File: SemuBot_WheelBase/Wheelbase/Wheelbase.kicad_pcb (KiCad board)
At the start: 2 copper layers, 100 x 80 mm, 120 parts, among them IC1 DRV8353FSRTAR, IC2 DRV8353FSRTAR, IC3 DRV8353FSRTAR, J1 10155435-00011LF, J10 B5B-XH-A_LF__SN_, J11 B5B-XH-A_LF__SN_, J12 B5B-XH-A_LF__SN_, J13 MTSW-104-09-L-S-400, J14 XT30PW-M, J15 MTSW-104-09-L-S-400, J2 MTSW-102-09-L-S-400, J3 MR30PW-M, J4 B5B-XH-A_LF__SN_, J5 B5B-XH-A_LF__SN_, J6 B5B-XH-A_LF__SN_, J7 MR30PW-M, J8 MR30PW-M, J9 DS1013-10SSIB1, Q1 AON7262E, Q10 AON7262E, Q11 AON7262E, Q12 AON7262E, Q13 AON7262E, Q14 AON7262E, Q15 AON7262E, Q19 AON7262E, Q2 AON7262E, Q20 AON7262E, Q21 AON7262E, Q3 AON7262E, Q4 AON7262E, Q5 AON7262E, Q6 AON7262E, Q7 AON7262E, Q8 AON7262E, Q9 AON7262E, U1 STM32F303RET6, U5 RT9013-33GB, Y2 X322516MLB4SI

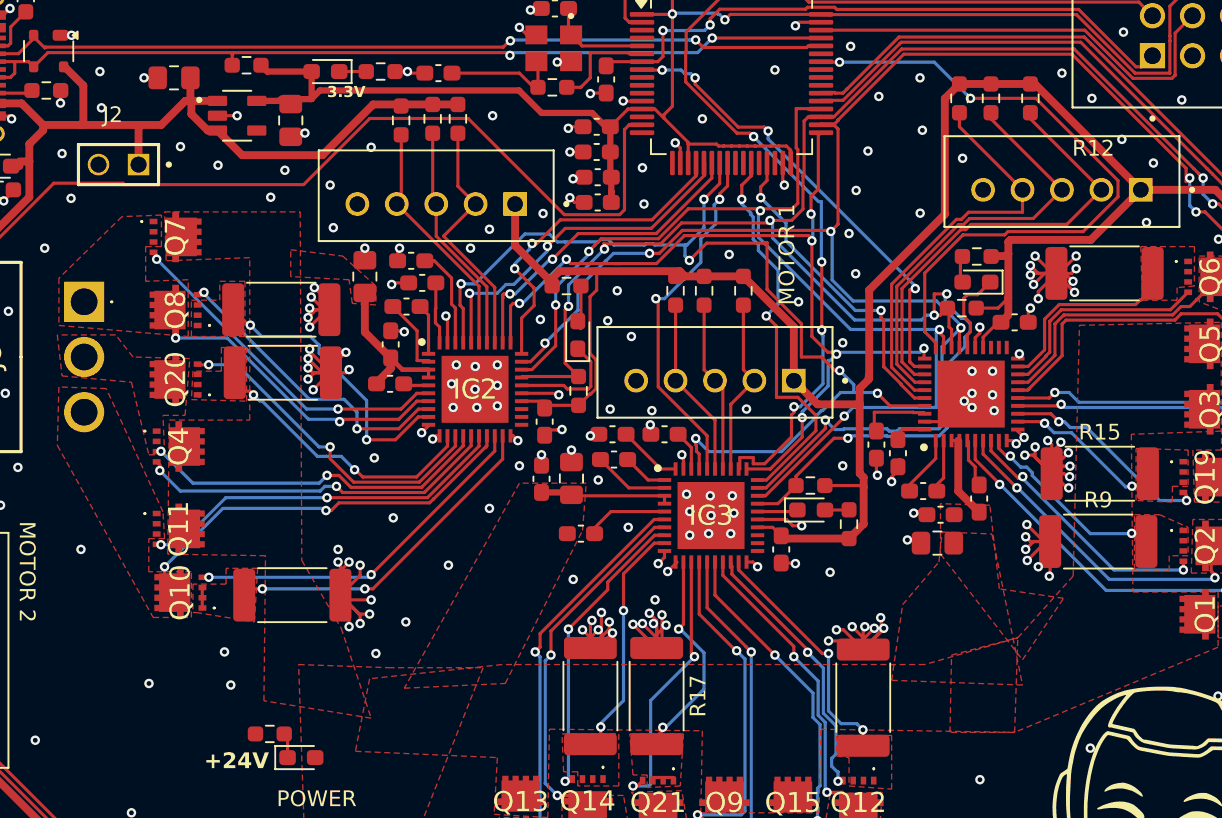
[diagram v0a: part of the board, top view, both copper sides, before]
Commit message: Wheelbase development and repo cleanup
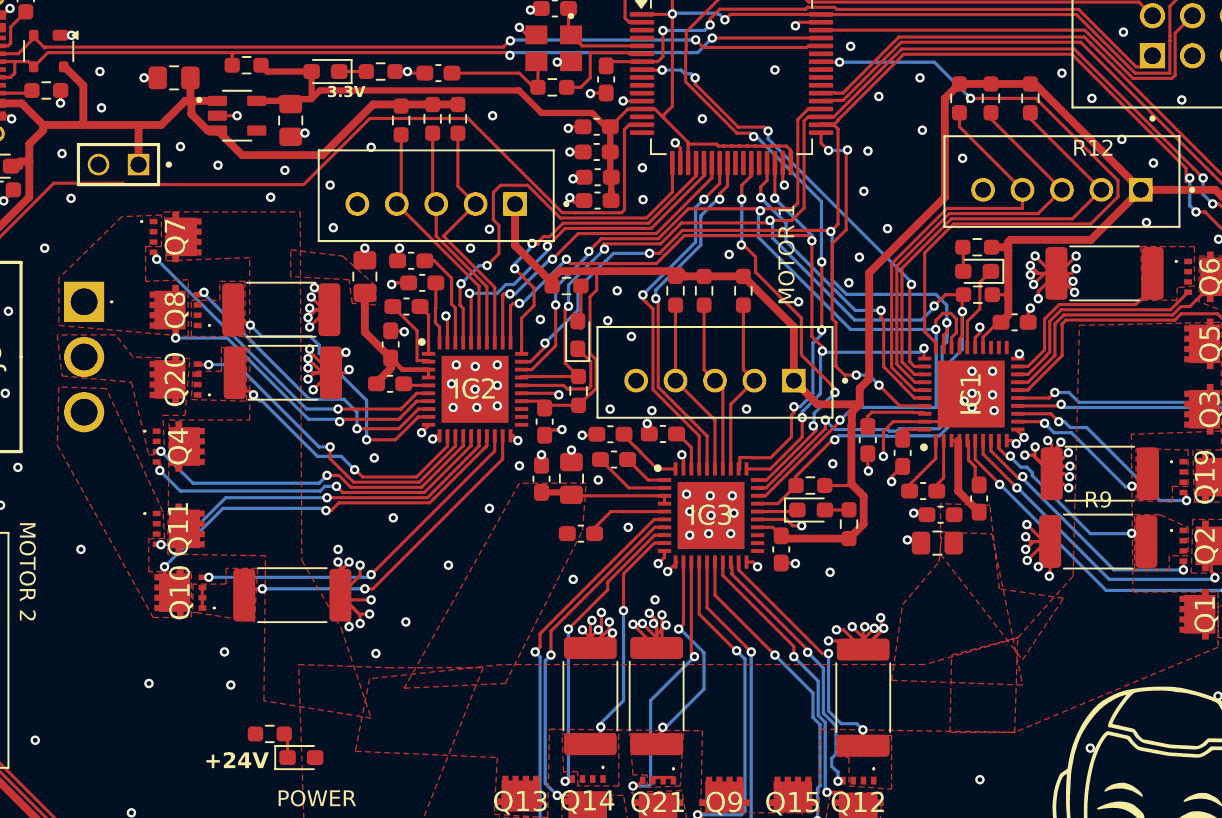
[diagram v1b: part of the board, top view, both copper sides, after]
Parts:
- moved R24 1.33 mm to (170.2, 88.6)
- moved D4 0.68 mm to (170.2, 87.1)
- moved C7 0.62 mm to (163.3, 97.8)
- moved R4 0.59 mm to (170.2, 85.6)
- moved C28 0.30 mm to (165.5, 98.6)
- moved C30 0.13 mm to (146.9, 97.5)
- moved C12 0.12 mm to (146.1, 82.6)
- moved C25 0.10 mm to (150.3, 97.4)
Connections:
- IC1 pad 27: /SPI_CLK -> /SPI_DATA
- IC1 pad 28: /SPI_DATA -> /SPI_MOSI
- IC1 pad 29: /SPI_MOSI -> /SPI_CLK
- IC1 pad 37: /nBRAKE -> /motor1_nBRAKE
- IC2 pad 37: /nBRAKE -> /motor2_nBRAKE
- IC3 pad 37: /nBRAKE -> /motor3_nBRAKE
- U1 pad 17: unconnected-(U1-PA3-Pad17) -> /motor2_nBRAKE
- U1 pad 23: /nBRAKE -> /motor3_nBRAKE
- U1 pad 30: unconnected-(U1-PB11-Pad30) -> /ENABLE
- U1 pad 33: /ENABLE -> /motor1_nBRAKE
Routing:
- net /nBRAKE: track 64.0 -> 0.00 mm, vias 6 -> 0
- net /motor2_nBRAKE: track 0.00 -> 26.0 mm, vias 0 -> 2
- net /motor1_nBRAKE: track 0.00 -> 23.4 mm, vias 0 -> 4
- net /motor3_nBRAKE: track 0.00 -> 22.9 mm, vias 0 -> 2
- net GND: track 176.0 -> 181.2 mm, vias 267 -> 266
- net /SPI_MOSI: track 67.4 -> 69.5 mm
- net /SPI_DATA: track 265.8 -> 264.0 mm
- net +5V: track 376.1 -> 374.4 mm
- net /ENABLE: track 56.5 -> 55.2 mm
- net /motor1_Cs: track 42.3 -> 43.0 mm
- net /Motor_1/HAL_2: track 26.9 -> 27.7 mm
- net /Motor_1/HAL_1: track 28.4 -> 29.2 mm
- net /Motor_1/HAL_3: track 26.2 -> 26.8 mm
- net /MOTOR3_PWM: track 40.1 -> 39.4 mm
- net /motor3_Cs: track 25.6 -> 25.4 mm, vias 2 -> 4

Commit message: Current sensing
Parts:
- removed D10, D11, D12: red, LED_SMD:LED_0603_1608Metric_Pad1.05x0.95mm_HandSolder
- removed D4, D5, D6: LED, LED_SMD:LED_0603_1608Metric_Pad1.05x0.95mm_HandSolder
- removed the R21 at (162.3, 64.8)
- removed the R22 at (169.6, 63.9)
- removed R23, R24, R25: 3.3K, Resistor_SMD:R_0603_1608Metric_Pad0.98x0.95mm_HandSolder
- removed the R3 at (144.9, 94.7)
- added C16: 220nF, Capacitor_SMD:C_0603_1608Metric_Pad1.08x0.95mm_HandSolder, F.Cu at (175.8, 80.0)
- added C22: 220nF, Capacitor_SMD:C_0603_1608Metric_Pad1.08x0.95mm_HandSolder, F.Cu at (143.0, 106.9)
- added C34: 220nF, Capacitor_SMD:C_0603_1608Metric_Pad1.08x0.95mm_HandSolder, F.Cu at (164.9, 111.6)
- added C35: 100nF, Capacitor_SMD:C_0603_1608Metric_Pad1.08x0.95mm_HandSolder, F.Cu at (175.9, 84.5)
- added C36: 100nF, Capacitor_SMD:C_0603_1608Metric_Pad1.08x0.95mm_HandSolder, F.Cu at (143.1, 104.7)
- added C37: 100nF, Capacitor_SMD:C_0603_1608Metric_Pad1.08x0.95mm_HandSolder, F.Cu at (161.5, 114.1)
- added C38: 100nF, Capacitor_SMD:C_0603_1608Metric_Pad1.08x0.95mm_HandSolder, F.Cu at (175.8, 81.5)
- added C39: 100nF, Capacitor_SMD:C_0603_1608Metric_Pad1.08x0.95mm_HandSolder, F.Cu at (143.1, 103.2)
- added C40: 100nF, Capacitor_SMD:C_0603_1608Metric_Pad1.08x0.95mm_HandSolder, F.Cu at (164.1, 114.6)
- added C50: 100nF, Capacitor_SMD:C_0603_1608Metric_Pad1.08x0.95mm_HandSolder, F.Cu at (166.1, 105.3)
- added C51: 100nF, Capacitor_SMD:C_0603_1608Metric_Pad1.08x0.95mm_HandSolder, F.Cu at (175.8, 83.0)
- added C52: 100nF, Capacitor_SMD:C_0603_1608Metric_Pad1.08x0.95mm_HandSolder, F.Cu at (143.1, 101.6)
- added C53: 100nF, Capacitor_SMD:C_0603_1608Metric_Pad1.08x0.95mm_HandSolder, F.Cu at (164.1, 116.1)
- added IC4: ADS131M03IRUKT, ADS131M:QFN40P300X300X80-21N-D, F.Cu at (180.1, 82.9)
- added IC5: ADS131M03IRUKT, ADS131M:QFN40P300X300X80-21N-D, F.Cu at (139.0, 105.1)
- added IC6: ADS131M03IRUKT, ADS131M:QFN40P300X300X80-21N-D, F.Cu at (168.2, 114.7)
- added R32: 1.5K, Resistor_SMD:R_0603_1608Metric_Pad0.98x0.95mm_HandSolder, F.Cu at (164.1, 93.5)
- added R33: 1.5K, Resistor_SMD:R_0603_1608Metric_Pad0.98x0.95mm_HandSolder, F.Cu at (135.8, 77.5)
- added R34: 1.5K, Resistor_SMD:R_0603_1608Metric_Pad0.98x0.95mm_HandSolder, F.Cu at (154.8, 98.4)
- added R45: 3.3K, Resistor_SMD:R_0603_1608Metric_Pad0.98x0.95mm_HandSolder, F.Cu at (105.6, 121.3)
- added Y1: ECS-2520MVLC-081.92-CN-TR, ECS-2520:OSC_ECS-2520MVLC-081.92-CN-TR, F.Cu at (168.6, 103.4)
- moved H4 113.4 mm to (200.0, 140.0)
- moved H2 85.2 mm to (110.0, 140.0)
- moved H1 67.1 mm to (118.0, 67.0)
- moved R22 31.9 mm to (173.0, 113.2)
- moved R21 27.2 mm to (135.9, 104.7)
- moved R35 20.4 mm to (164.1, 96.0), turned to 180 degrees
- moved R29 17.6 mm to (164.1, 91.0), turned to 180 degrees
- moved H3 15.8 mm to (200.0, 67.0)
- moved R3 15.4 mm to (185.2, 82.3), turned to -90 degrees
- moved D7 15.4 mm to (124.6, 133.1)
- moved R18 14.9 mm to (122.7, 131.2)
- moved J15 14.6 mm to (163.4, 64.2)
- moved J4 13.6 mm to (169.3, 93.5), turned to -90 degrees
- moved C33 13.1 mm to (144.7, 113.4)
- moved C23 13.0 mm to (142.8, 113.3)
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- renumbered R33 to R21, R34 to R22, R32 to R3
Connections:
- C18 pad 1: +5V -> +3.3V
- C24 pad 1: +5V -> +3.3V
- C6 pad 1: +5V -> +3.3V
- IC1 pad 21: unconnected-(IC1-SOC-Pad21) -> /Motor_1/SOC
- IC1 pad 22: unconnected-(IC1-SOB-Pad22) -> /Motor_1/SOB
- IC1 pad 23: unconnected-(IC1-SOA-Pad23) -> /Motor_1/SOA
- IC1 pad 24: +5V -> +3.3V
- IC1 pad 26: Net-(D4-K) -> Net-(IC1-NFAULT)
- IC2 pad 21: unconnected-(IC2-SOC-Pad21) -> /Motor_2/SOC
- IC2 pad 22: unconnected-(IC2-SOB-Pad22) -> /Motor_2/SOB
- IC2 pad 23: unconnected-(IC2-SOA-Pad23) -> /Motor_2/SOA
- IC2 pad 24: +5V -> +3.3V
- IC2 pad 26: Net-(D5-K) -> Net-(IC2-NFAULT)
- IC3 pad 21: unconnected-(IC3-SOC-Pad21) -> /Motor_3/SOC
- IC3 pad 22: unconnected-(IC3-SOB-Pad22) -> /Motor_3/SOB
- IC3 pad 23: unconnected-(IC3-SOA-Pad23) -> /Motor_3/SOA
- IC3 pad 24: +5V -> +3.3V
- IC3 pad 26: Net-(D6-K) -> Net-(IC3-NFAULT)
- J4 pad 2: /Motor_1/HAL_1 -> /Motor_1/HAL_3
- J4 pad 4: /Motor_1/HAL_3 -> /Motor_1/HAL_1
- R21 pad 1: /Motor_2/HAL_2 -> Net-(IC5-~{SYNC_}/_~{RESET})
- R21 pad 2: +5V -> +3.3V
- R22 pad 1: /Motor_3/HAL_2 -> Net-(IC6-~{SYNC_}/_~{RESET})
- R22 pad 2: +5V -> +3.3V
- R3 pad 1: /Motor_1/HAL_2 -> Net-(IC4-~{SYNC_}/_~{RESET})
- R3 pad 2: +5V -> +3.3V
- R4 pad 1: Net-(D4-A) -> Net-(IC1-NFAULT)
- R4 pad 2: +5V -> +3.3V
- R7 pad 1: Net-(D5-A) -> Net-(IC2-NFAULT)
- R7 pad 2: +5V -> +3.3V
- R8 pad 1: Net-(D6-A) -> Net-(IC3-NFAULT)
- R8 pad 2: +5V -> +3.3V
- U1 pad 14: unconnected-(U1-PA0-Pad14) -> /motor2_DRDY
- U1 pad 16: unconnected-(U1-PA2-Pad16) -> /motor2_adc
- U1 pad 28: unconnected-(U1-PB2-Pad28) -> /motor3_adc
- U1 pad 29: /MOTOR1_DIR -> /motor3_DRDY
- U1 pad 37: /CS_ENC_3 -> /MOTOR1_DIR
- U1 pad 38: /CS_ENC_1 -> /CS_ENC_3
- U1 pad 39: unconnected-(U1-PC8-Pad39) -> /CS_ENC_1
- U1 pad 40: unconnected-(U1-PC9-Pad40) -> /motor1_DRDY
- U1 pad 41: unconnected-(U1-PA8-Pad41) -> /MOTOR1_PWM
- U1 pad 43: unconnected-(U1-PA10-Pad43) -> /motor1_adc
- U1 pad 55: /motor2_led -> unconnected-(U1-PB3-Pad55)
- U1 pad 56: /motor3_led -> unconnected-(U1-PB4-Pad56)
- U1 pad 57: /motor1_led -> unconnected-(U1-PB5-Pad57)
- U1 pad 8: /MOTOR1_PWM -> unconnected-(U1-PC0-Pad8)
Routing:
- net +3.3V: track 113.7 -> 281.9 mm, vias 2 -> 8
- net /SPI_DATA: track 264.0 -> 352.6 mm, vias 8 -> 14
- net /adc_CLK: track 0.00 -> 72.4 mm, vias 0 -> 4
- net /SPI_MOSI: track 69.5 -> 128.7 mm, vias 5 -> 10
- net +5V: track 374.4 -> 316.7 mm, vias 0 -> 4
- net /SPI_CLK: track 256.9 -> 311.3 mm, vias 7 -> 15
- net /motor3_adc: track 0.00 -> 43.2 mm, vias 0 -> 6
- net /motor2_adc: track 0.00 -> 40.6 mm, vias 0 -> 2
- net /motor3_DRDY: track 0.00 -> 39.4 mm, vias 0 -> 6
- net /motor2_DRDY: track 0.00 -> 37.8 mm, vias 0 -> 2
- net /motor1_DRDY: track 0.00 -> 31.3 mm, vias 0 -> 2
- net /motor1_adc: track 0.00 -> 27.2 mm, vias 0 -> 2
- net GND: track 181.2 -> 207.7 mm, vias 266 -> 303
- net /ENABLE: track 55.2 -> 74.8 mm, vias 7 -> 13
- net /motor3_led: track 17.8 -> 0.00 mm
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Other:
- board size 100 x 80 mm -> 110 x 90 mm
- board text added: "ENCODER"
- board text removed: "BRWN"
- board text removed: "M1"
- board text removed: "M2"
- board text removed: "M3"
- board text removed: "ORANGE"
- board text removed: "POWER"

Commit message: Current sensing, + changing encoder pins
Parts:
- moved R45 51.6 mm to (148.3, 92.5), turned to 90 degrees
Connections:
- net /MCU_CS renamed /SPI3_NSS
- J10 pad 2: /SPI_DATA -> /SSI_DATA
- J10 pad 3: /SPI_CLK -> /SSI_CLK
- J11 pad 2: /SPI_DATA -> /SSI_DATA
- J11 pad 3: /SPI_CLK -> /SSI_CLK
- J12 pad 2: /SPI_DATA -> /SSI_DATA
- J12 pad 3: /SPI_CLK -> /SSI_CLK
- U1 pad 54: unconnected-(U1-PD2-Pad54) -> /SSI_CLK
- U1 pad 55: unconnected-(U1-PB3-Pad55) -> /SSI_DATA
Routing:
- net /SSI_CLK: track 0.00 -> 246.1 mm, vias 0 -> 2
- net /SSI_DATA: track 0.00 -> 240.5 mm, vias 0 -> 3
- net /SPI_DATA: track 352.6 -> 127.6 mm, vias 14 -> 13
- net /SPI_CLK: track 311.3 -> 125.2 mm, vias 15 -> 12
